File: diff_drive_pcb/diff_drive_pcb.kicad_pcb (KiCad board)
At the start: 2 copper layers, 13 parts, among them J1 Conn_01x02_Pin, J10 Conn_01x02_Pin, J2 Conn_01x04_Socket, J3 Conn_01x02_Pin, J4 Conn_01x04_Socket, J5 Conn_01x02_Pin, J6 Conn_01x04_Socket, J7 Conn_01x02_Pin, J8 Conn_01x04_Socket, J9 Conn_01x02_Pin, U1 TB6612FNG, U2 TB6612FNG, U3 Teensy4.1

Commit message: PCB v1.0 developed
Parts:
- added BZ1: Buzzer, Buzzer_Beeper:Buzzer_TDK_PS1240P02BT_D12.2mm_H6.5mm, F.Cu at (167.5, 143.9)
- added BZ3: Buzzer, Buzzer_Beeper:Buzzer_TDK_PS1240P02BT_D12.2mm_H6.5mm, F.Cu at (149.5, 143.9)
- added D1: 1N5400, Diode_THT:D_DO-201AD_P15.24mm_Horizontal, F.Cu at (204.7, 56.4)
- added D2: 1N5400, Diode_THT:D_DO-201AD_P15.24mm_Horizontal, F.Cu at (210.6, 56.4)
- added D3: status_led1, Connector_PinHeader_2.54mm:PinHeader_1x02_P2.54mm_Vertical, F.Cu at (175.5, 65.9)
- added D4: status_led2, Connector_PinHeader_2.54mm:PinHeader_1x02_P2.54mm_Vertical, F.Cu at (175.5, 69.9)
- added D5: status_led3, Connector_PinHeader_2.54mm:PinHeader_1x02_P2.54mm_Vertical, F.Cu at (175.5, 73.9)
- added D6: headlight, Connector_PinHeader_2.54mm:PinHeader_1x02_P2.54mm_Vertical, F.Cu at (138.5, 102.9)
- added J11: Motor_Break_SW, Connector_PinHeader_2.54mm:PinHeader_1x03_P2.54mm_Vertical, F.Cu at (146.0, 120.5)
- added J12: 5v_out_1, Connector_JST:JST_XH_B2B-XH-A_1x02_P2.50mm_Vertical, F.Cu at (196.0, 57.4)
- added J13: 5v_out_2, Connector_JST:JST_XH_B2B-XH-A_1x02_P2.50mm_Vertical, F.Cu at (196.0, 64.4)
- added J14: 5v_out_3, Connector_JST:JST_XH_B2B-XH-A_1x02_P2.50mm_Vertical, F.Cu at (196.0, 71.4)
- added J15: 5v_out_4, Connector_JST:JST_XH_B2B-XH-A_1x02_P2.50mm_Vertical, F.Cu at (196.0, 78.4)
- added J16: 3v3_out_1, Connector_JST:JST_XH_B2B-XH-A_1x02_P2.50mm_Vertical, F.Cu at (187.0, 71.4)
- added J17: 3v3_out_2, Connector_JST:JST_XH_B2B-XH-A_1x02_P2.50mm_Vertical, F.Cu at (187.0, 78.4)
- added J18: 3v3_out_3, Connector_JST:JST_XH_B2B-XH-A_1x02_P2.50mm_Vertical, F.Cu at (187.0, 57.4)
- added J19: 3v3_out_4, Connector_JST:JST_XH_B2B-XH-A_1x02_P2.50mm_Vertical, F.Cu at (187.0, 64.4)
- added R1: 1K, Resistor_THT:R_Axial_DIN0204_L3.6mm_D1.6mm_P2.54mm_Vertical, F.Cu at (165.0, 66.6)
- added R2: 1K, Resistor_THT:R_Axial_DIN0204_L3.6mm_D1.6mm_P2.54mm_Vertical, F.Cu at (165.0, 69.8)
- added R3: 1K, Resistor_THT:R_Axial_DIN0204_L3.6mm_D1.6mm_P2.54mm_Vertical, F.Cu at (165.0, 72.9)
- added U4: TOF_front_left, Connector_JST:JST_XH_B6B-XH-AM_1x06_P2.50mm_Vertical, F.Cu at (113.1, 105.9)
- added U5: Tof_back_left, Connector_JST:JST_XH_B6B-XH-AM_1x06_P2.50mm_Vertical, F.Cu at (113.1, 123.4)
- added U6: Tof_front_right, Connector_JST:JST_XH_B6B-XH-AM_1x06_P2.50mm_Vertical, F.Cu at (113.1, 114.9)
- added U7: Tof_back_right, Connector_JST:JST_XH_B6B-XH-AM_1x06_P2.50mm_Vertical, F.Cu at (113.0, 132.9)
- added U8: MPU9250, Connector_PinHeader_2.54mm:PinHeader_1x10_P2.54mm_Vertical, F.Cu at (181.0, 85.4)
- J1: value Conn_01x02_Pin -> P_M1
- J10: value Conn_01x02_Pin -> 12V_IN
- J2: value Conn_01x04_Socket -> Encoder_M1
- J3: value Conn_01x02_Pin -> P_M2
- J4: value Conn_01x04_Socket -> Encoder_M2
- J5: value Conn_01x02_Pin -> P_M3
- J6: value Conn_01x04_Socket -> Encoder_M3
- J7: value Conn_01x02_Pin -> P_M4
- J8: value Conn_01x04_Socket -> Encoder_M4
- J9: value Conn_01x02_Pin -> 5V_IN
- U1: value TB6612FNG -> Motor Driver1; footprint Package_SO:SSOP-24_5.3x8.2mm_P0.65mm -> TB6612FNG:TB6612FNG breakout board
- U2: value TB6612FNG -> Motor Driver 2; footprint Package_SO:SSOP-24_5.3x8.2mm_P0.65mm -> TB6612FNG:TB6612FNG breakout board
- moved J5 89.5 mm to (109.5, 85.8)
- moved J8 87.6 mm to (182.5, 109.6), turned to -90 degrees
- moved J7 79.5 mm to (108.5, 96.8), turned to 90 degrees
- moved J2 64.7 mm to (172.5, 93.5), turned to -90 degrees
- moved J10 46.5 mm to (125.5, 40.5)
- moved J9 44.0 mm to (117.0, 40.5)
- moved U2 43.0 mm to (128.4, 90.0)
- moved J4 41.7 mm to (182.5, 93.4)
- moved J3 22.4 mm to (108.5, 77.2)
- moved J1 20.9 mm to (109.5, 65.8), turned to -90 degrees
- moved J6 16.2 mm to (172.5, 109.5)
- moved U3 10.7 mm to (153.9, 86.7)
- moved U1 6.47 mm to (128.4, 68.7)
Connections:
- U1 pad 1: /M1+ -> +12V
- U1 pad 10: Net-(U1-PGND2-Pad10) -> M1_ctrl_B
- U1 pad 11: /M2+ -> M1_ctrl_A
- U1 pad 12: /M2+ -> /Brk_sw
- U1 pad 13: unconnected-(U1-VM2-Pad13) -> M2_ctrl_A
- U1 pad 14: unconnected-(U1-VM3-Pad14) -> M2_ctrl_B
- U1 pad 15: unconnected-(U1-PWMB-Pad15) -> M2_ctrl_PWM
- U1 pad 16: unconnected-(U1-BIN2-Pad16) -> GND
- U1 pad 2: /M1+ -> +5V
- U1 pad 4: GND -> /M1+
- U1 pad 6: /M1- -> /M2-
- U1 pad 7: /M2- -> /M2+
- U1 pad 8: /M2- -> GND
- U1 pad 9: Net-(U1-PGND2-Pad10) -> M1_ctrl_PWM
- U2 pad 1: /M4+ -> +12V
- U2 pad 10: Net-(U2-PGND2-Pad10) -> M3_ctrl_B
- U2 pad 11: /M3+ -> M3_ctrl_A
- U2 pad 12: /M3+ -> /Brk_sw
- U2 pad 13: unconnected-(U2-VM2-Pad13) -> M4_ctrl_A
- U2 pad 14: unconnected-(U2-VM3-Pad14) -> M4_ctrl_B
- U2 pad 15: unconnected-(U2-PWMB-Pad15) -> M4_ctrl_PWM
- U2 pad 16: unconnected-(U2-BIN2-Pad16) -> GND
- U2 pad 2: /M4+ -> +5V
- U2 pad 4: GND -> /M3+
- U2 pad 5: /M4- -> /M3-
- U2 pad 7: /M3- -> /M4+
- U2 pad 8: /M3- -> GND
- U2 pad 9: Net-(U2-PGND2-Pad10) -> M3_ctrl_PWM
- U3 pad 10: M4_encB -> M3_ctrl_PWM
- U3 pad 11: M4_encA -> M3_ctrl_B
- U3 pad 12: unconnected-(U3-10_CS_MQSR-Pad12) -> M3_ctrl_A
- U3 pad 13: unconnected-(U3-11_MOSI_CTX1-Pad13) -> M4_ctrl_A
- U3 pad 14: unconnected-(U3-12_MISO_MQSL-Pad14) -> M4_ctrl_B
- U3 pad 16: unconnected-(U3-24_A10_TX6_SCL2-Pad16) -> M4_ctrl_PWM
- U3 pad 19: unconnected-(U3-27_A13_SCK1-Pad19) -> HEADLIGHTS
- U3 pad 20: unconnected-(U3-28_RX7-Pad20) -> XSHUT1
- U3 pad 21: unconnected-(U3-29_TX7-Pad21) -> XSHUT2
- U3 pad 22: unconnected-(U3-30_CRX3-Pad22) -> XSHUT3
- U3 pad 23: unconnected-(U3-31_CTX3-Pad23) -> XSHUT4
- U3 pad 24: unconnected-(U3-32_OUT1B-Pad24) -> /MD_stby
- U3 pad 25: unconnected-(U3-33_MCLK2-Pad25) -> M4_encA
- U3 pad 26: unconnected-(U3-34_RX8-Pad26) -> M4_encB
- U3 pad 27: unconnected-(U3-35_TX8-Pad27) -> M3_encA
- U3 pad 28: unconnected-(U3-36_CS-Pad28) -> M3_encB
- U3 pad 29: unconnected-(U3-37_CS-Pad29) -> M2_encA
- U3 pad 30: unconnected-(U3-38_CS1_IN1-Pad30) -> M2_encB
- U3 pad 31: unconnected-(U3-39_MISO1_OUT1A-Pad31) -> M1_encA
- U3 pad 32: unconnected-(U3-40_A16-Pad32) -> M1_encB
- U3 pad 38: unconnected-(U3-16_A2_RX4_SCL1-Pad38) -> MPU_SCL
- U3 pad 39: unconnected-(U3-17_A3_TX4_SDA1-Pad39) -> MPU_SDA
- U3 pad 4: M1_encB -> M1_ctrl_PWM
- U3 pad 42: unconnected-(U3-20_A6_TX5_LRCLK1-Pad42) -> STATUS_LED3
- U3 pad 43: unconnected-(U3-21_A7_RX5_BCLK1-Pad43) -> STATUS_LED2
- U3 pad 44: unconnected-(U3-22_A8_CTX1-Pad44) -> STATUS_LED1
- U3 pad 45: unconnected-(U3-23_A9_CRX1_MCLK1-Pad45) -> Buzzer_ctl
- U3 pad 46: unconnected-(U3-3V3-Pad46) -> +3V3
- U3 pad 5: M1_encA -> M1_ctrl_B
- U3 pad 6: M2_encB -> M1_ctrl_A
- U3 pad 7: M2_encA -> M2_ctrl_A
- U3 pad 8: M3_encB -> M2_ctrl_B
- U3 pad 9: M3_encA -> M2_ctrl_PWM
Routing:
- net GND: track 0.00 -> 466.7 mm
- net +5V: track 0.00 -> 399.4 mm
- net Buzzer_ctl: track 0.00 -> 127.4 mm
- net MPU_SDA: track 0.00 -> 101.6 mm
- net MPU_SCL: track 0.00 -> 98.0 mm
- net +3V3: track 0.00 -> 78.7 mm
- net /Brk_sw: track 0.00 -> 69.7 mm, vias 0 -> 1
- net +12V: track 0.00 -> 45.5 mm
- net Net-(D2-K): track 0.00 -> 44.5 mm
- net M4_encA: track 0.00 -> 30.2 mm
- net XSHUT4: track 0.00 -> 29.7 mm
- net M2_encA: track 0.00 -> 28.5 mm
- net Net-(D1-K): track 0.00 -> 27.6 mm
- net XSHUT3: track 0.00 -> 25.8 mm
- net M2_encB: track 0.00 -> 24.2 mm
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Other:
- board outline added: 114.5 x 119.5 mm
- board text added: "+12V_IN"
- board text added: "+3V3"
- board text added: "+5V"
- board text added: "+5V IN"
- board text added: "- +"
- board text added: "BL"
- board text added: "BR"
- board text added: "Brk_sw"
- board text added: "DIFF DRIVE CONTROLLER"
- board text added: "Designed By ShenLong"
- board text added: "E_M1"
- board text added: "E_M2"
- board text added: "E_M3"
- board text added: "E_M4"
- board text added: "FL"
- board text added: "FR"
- board text added: "L1"
- board text added: "L2"
- board text added: "L3"
- board text added: "M1_PWR"
- board text added: "M2_PWR"
- board text added: "M3_PWR"
- board text added: "M4_PWR"
- board text added: "MC_sw"
- board text added: "MOTOR ENCODER"
- board text added: "MPU_9250"
- board text added: "Motor_Break SW"
- board text added: "POWER OUTPUT"
- board text added: "Time of Flight"
- board text added: "v1.0"

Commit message: Updated Schematic
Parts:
- removed D1, D2: 1N5400, Diode_THT:D_DO-201AD_P15.24mm_Horizontal
- removed J12: 5v_out_1, Connector_JST:JST_XH_B2B-XH-A_1x02_P2.50mm_Vertical
- removed J13: 5v_out_2, Connector_JST:JST_XH_B2B-XH-A_1x02_P2.50mm_Vertical
- removed J14: 5v_out_3, Connector_JST:JST_XH_B2B-XH-A_1x02_P2.50mm_Vertical
- removed J15: 5v_out_4, Connector_JST:JST_XH_B2B-XH-A_1x02_P2.50mm_Vertical
- removed J16: 3v3_out_1, Connector_JST:JST_XH_B2B-XH-A_1x02_P2.50mm_Vertical
- removed J17: 3v3_out_2, Connector_JST:JST_XH_B2B-XH-A_1x02_P2.50mm_Vertical
- removed J18: 3v3_out_3, Connector_JST:JST_XH_B2B-XH-A_1x02_P2.50mm_Vertical
- removed J19: 3v3_out_4, Connector_JST:JST_XH_B2B-XH-A_1x02_P2.50mm_Vertical
- added D7: headlight, Connector_PinHeader_2.54mm:PinHeader_1x02_P2.54mm_Vertical, F.Cu at (92.5, 121.0)
- added Q2: IRLZ24, Package_TO_SOT_THT:TO-220-3_Vertical, F.Cu at (86.4, 105.5)
- added R4: 10k, Resistor_THT:R_Axial_DIN0204_L3.6mm_D1.6mm_P5.08mm_Horizontal, F.Cu at (95.5, 108.0)
- added R5: 100, Resistor_THT:R_Axial_DIN0204_L3.6mm_D1.6mm_P5.08mm_Horizontal, F.Cu at (93.2, 108.8)
- added R6: 100, Resistor_THT:R_Axial_DIN0204_L3.6mm_D1.6mm_P5.08mm_Horizontal, F.Cu at (89.2, 108.8)
- U1: value Motor Driver1 -> Motor Driver 1; footprint TB6612FNG:TB6612FNG breakout board -> MDD3A:MDD3A
- U2: footprint TB6612FNG:TB6612FNG breakout board -> MDD3A:MDD3A
- moved J11 110.6 mm to (73.1, 37.3), turned to 180 degrees
- moved U6 91.4 mm to (182.5, 55.4), turned to -90 degrees
- moved U7 90.9 mm to (182.5, 74.2), turned to -90 degrees
- moved U4 79.4 mm to (174.5, 55.5), turned to -90 degrees
- moved U5 78.6 mm to (174.5, 74.2), turned to -90 degrees
- moved J4 62.1 mm to (121.0, 101.8), turned to 90 degrees
- moved J2 57.5 mm to (115.0, 94.3)
- moved BZ1 48.3 mm to (129.5, 114.1), turned to -90 degrees
- moved D6 48.2 mm to (92.5, 117.2), turned to -90 degrees
- moved J9 47.3 mm to (163.8, 33.1), turned to -90 degrees
- moved U1 42.8 mm to (94.6, 42.3), turned to -90 degrees
- moved J1 41.6 mm to (83.4, 33.4)
- moved U2 40.9 mm to (94.4, 67.2), turned to -90 degrees
- moved J3 38.5 mm to (82.9, 48.4), turned to -90 degrees
- moved J5 37.3 mm to (83.1, 59.4)
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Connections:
- D6 pad 2: HEADLIGHTS -> Net-(D6-A)
- J11 pad 3: +5V -> GND
- U1 pad 1: +12V -> M1_ctrl_A
- U1 pad 10: M1_ctrl_B -> /M2-
- U1 pad 11: M1_ctrl_A -> +12V
- U1 pad 2: +5V -> M1_ctrl_B
- U1 pad 4: /M1+ -> /Brk_sw
- U1 pad 5: /M1- -> M2_ctrl_A
- U1 pad 6: /M2- -> M2_ctrl_B
- U1 pad 7: /M2+ -> /M1+
- U1 pad 8: GND -> /M1-
- U1 pad 9: M1_ctrl_PWM -> /M2+
- U2 pad 1: +12V -> M3_ctrl_A
- U2 pad 10: M3_ctrl_B -> /M4-
- U2 pad 11: M3_ctrl_A -> +12V
- U2 pad 2: +5V -> M3_ctrl_B
- U2 pad 4: /M3+ -> /Brk_sw
- U2 pad 5: /M3- -> M4_ctrl_A
- U2 pad 6: /M4- -> M4_ctrl_B
- U2 pad 7: /M4+ -> /M3+
- U2 pad 8: GND -> /M3-
- U2 pad 9: M3_ctrl_PWM -> /M4+
- U3 pad 10: M3_ctrl_PWM -> unconnected-(U3-8_TX2_IN1-Pad10)
- U3 pad 11: M3_ctrl_B -> M3_ctrl_A
- U3 pad 12: M3_ctrl_A -> M3_ctrl_B
- U3 pad 16: M4_ctrl_PWM -> unconnected-(U3-24_A10_TX6_SCL2-Pad16)
- U3 pad 20: XSHUT1 -> M1_encA
- U3 pad 21: XSHUT2 -> M1_encB
- U3 pad 22: XSHUT3 -> M2_encA
- U3 pad 23: XSHUT4 -> M2_encB
- U3 pad 29: M2_encA -> XSHUT4
- U3 pad 30: M2_encB -> XSHUT3
- U3 pad 31: M1_encA -> XSHUT2
- U3 pad 32: M1_encB -> XSHUT1
- U3 pad 4: M1_ctrl_PWM -> unconnected-(U3-2_OUT2-Pad4)
- U3 pad 48: unconnected-(U3-VIN-Pad48) -> +5V
- U3 pad 5: M1_ctrl_B -> M1_ctrl_A
- U3 pad 6: M1_ctrl_A -> M1_ctrl_B
- U3 pad 9: M2_ctrl_PWM -> unconnected-(U3-7_RX2_OUT1A-Pad9)
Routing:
- net GND: track 466.7 -> 0.00 mm
- net +5V: track 399.4 -> 0.00 mm
- net Buzzer_ctl: track 127.4 -> 0.00 mm
- net MPU_SDA: track 101.6 -> 0.00 mm
- net MPU_SCL: track 98.0 -> 0.00 mm
- net +3V3: track 78.7 -> 0.00 mm
- net /Brk_sw: track 69.7 -> 0.00 mm, vias 1 -> 0
- net +12V: track 45.5 -> 0.00 mm
- net Net-(D2-K): track 44.5 -> 0.00 mm
- net M4_encA: track 30.2 -> 0.00 mm
- net XSHUT4: track 29.7 -> 0.00 mm
- net M2_encA: track 28.5 -> 0.00 mm
- net Net-(D1-K): track 27.6 -> 0.00 mm
- net XSHUT3: track 25.8 -> 0.00 mm
- net M2_encB: track 24.2 -> 0.00 mm
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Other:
- board outline removed
- board text added: "STATUS LED"
- board text removed: "+12V_IN"
- board text removed: "+3V3"
- board text removed: "+5V"
- board text removed: "+5V IN"
- board text removed: "- +"
- board text removed: "Brk_sw"
- board text removed: "DIFF DRIVE CONTROLLER"
- board text removed: "Designed By ShenLong"
- board text removed: "E_M1"
- board text removed: "E_M2"
- board text removed: "E_M3"
- board text removed: "E_M4"
- board text removed: "L1"
- board text removed: "L2"
- board text removed: "L3"
- board text removed: "M1_PWR"
- board text removed: "M2_PWR"
- board text removed: "M3_PWR"
- board text removed: "M4_PWR"
- board text removed: "MC_sw"
- board text removed: "MOTOR ENCODER"
- board text removed: "MPU_9250"
- board text removed: "Motor_Break SW"
- board text removed: "POWER OUTPUT"
- board text removed: "Time of Flight"
- board text removed: "v1.0"

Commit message: Rev 2.1 pcb design
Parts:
- added J12: POWER_SW, Connector_JST:JST_XH_B2B-XH-AM_1x02_P2.50mm_Vertical, F.Cu at (125.4, 61.9)
- moved Q2 103.9 mm to (184.5, 71.2)
- moved D6 103.9 mm to (190.6, 83.0)
- moved D7 103.9 mm to (190.6, 86.7)
- moved R4 103.9 mm to (193.6, 73.7)
- moved R5 103.9 mm to (191.3, 74.5)
- moved R6 103.9 mm to (187.3, 74.5)
- moved U6 103.4 mm to (108.5, 127.5), turned to 0 degrees
- moved U7 99.9 mm to (108.4, 141.2), turned to 0 degrees
- moved U4 92.7 mm to (108.5, 120.6), turned to 0 degrees
- moved U5 89.3 mm to (108.5, 134.3), turned to 0 degrees
- moved J11 80.0 mm to (129.0, 94.5)
- moved J9 60.8 mm to (110.7, 62.8), turned to 180 degrees
- moved J4 58.6 mm to (179.5, 98.9), turned to -90 degrees
- moved J2 54.8 mm to (169.6, 98.9)
- moved J1 48.1 mm to (99.7, 78.7)
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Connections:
- J9 pad 1: +5V -> (no net)
- J9 pad 2: GND -> (no net)
- U3 pad 10: unconnected-(U3-8_TX2_IN1-Pad10) -> /MD_stby
- U3 pad 19: HEADLIGHTS -> XSHUT1
- U3 pad 20: M1_encA -> XSHUT2
- U3 pad 21: M1_encB -> XSHUT3
- U3 pad 22: M2_encA -> XSHUT4
- U3 pad 23: M2_encB -> Buzzer_ctl
- U3 pad 24: /MD_stby -> unconnected-(U3-32_OUT1B-Pad24)
- U3 pad 29: XSHUT4 -> M2_encA
- U3 pad 30: XSHUT3 -> M2_encB
- U3 pad 31: XSHUT2 -> M1_encA
- U3 pad 32: XSHUT1 -> M1_encB
- U3 pad 41: unconnected-(U3-19_A5_SCL-Pad41) -> STATUS_LED3
- U3 pad 42: STATUS_LED3 -> STATUS_LED2
- U3 pad 43: STATUS_LED2 -> STATUS_LED1
- U3 pad 44: STATUS_LED1 -> HEADLIGHTS
- U3 pad 45: Buzzer_ctl -> unconnected-(U3-23_A9_CRX1_MCLK1-Pad45)
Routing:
- net GND: track 0.00 -> 336.4 mm
- net +5V: track 0.00 -> 282.8 mm, vias 0 -> 2
- net MPU_SDA: track 0.00 -> 104.7 mm
- net MPU_SCL: track 0.00 -> 99.9 mm
- net HEADLIGHTS: track 0.00 -> 54.3 mm
- net Buzzer_ctl: track 0.00 -> 41.5 mm
- net /Brk_sw: track 0.00 -> 41.2 mm
- net +12V: track 0.00 -> 36.8 mm
- net XSHUT4: track 0.00 -> 31.6 mm
- net M2_encB: track 0.00 -> 28.4 mm
- net M2_encA: track 0.00 -> 28.2 mm
- net XSHUT3: track 0.00 -> 27.3 mm
- net M4_encA: track 0.00 -> 26.8 mm
- net M4_encB: track 0.00 -> 26.8 mm
- net M3_ctrl_A: track 0.00 -> 25.9 mm
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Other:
- board outline added: 111 x 110.7 mm
- board text added: "HEADLIGHT"
- board text added: "IMU"

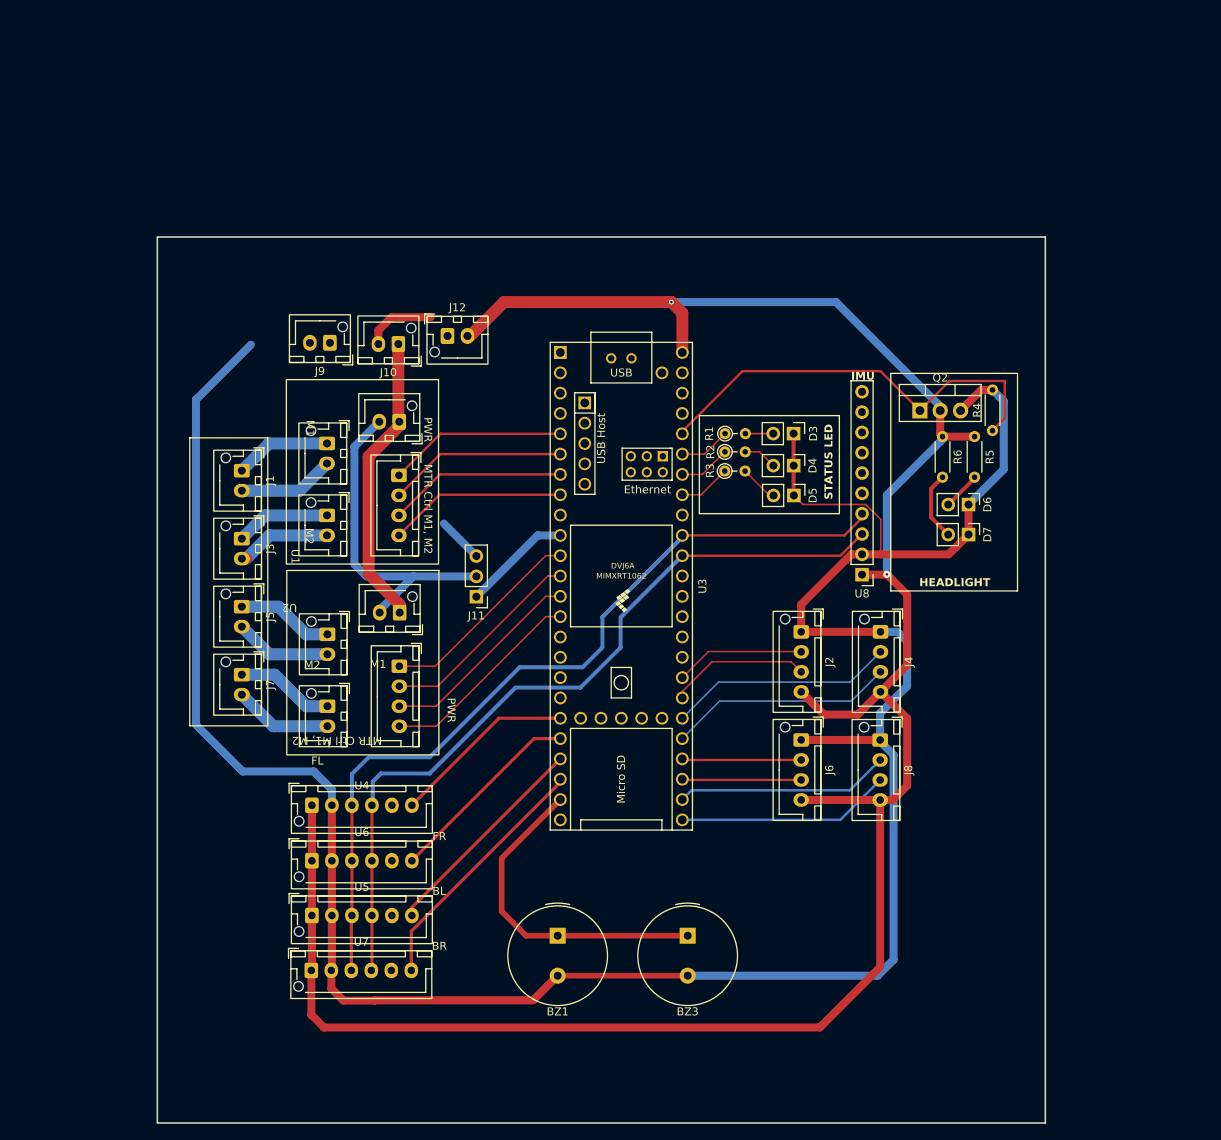
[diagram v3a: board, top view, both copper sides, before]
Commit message: Cleaned up PCB and adjusted size
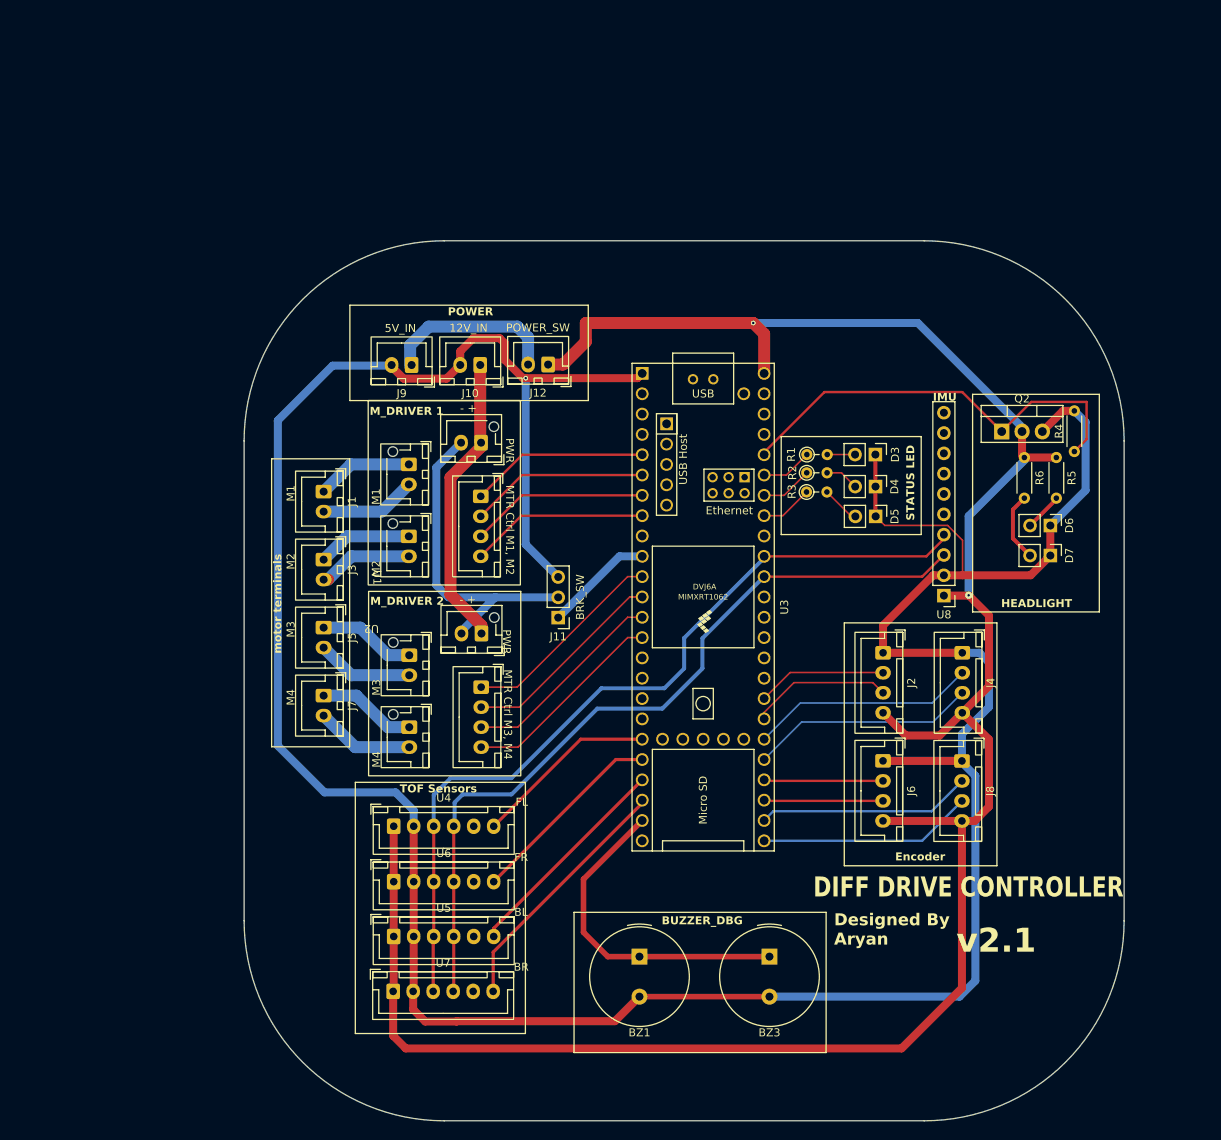
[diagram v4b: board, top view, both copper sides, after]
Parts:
- J1, J10, J12, J3, J5, J7, J9: footprint Connector_JST:JST_XH_B2B-XH-AM_1x02_P2.50mm_Vertical -> Connector_JST:JST_XH_B2B-XH-A_1x02_P2.50mm_Vertical
- J2, J4, J6, J8: footprint Connector_JST:JST_XH_B4B-XH-AM_1x04_P2.50mm_Vertical -> Connector_JST:JST_XH_B4B-XH-A_1x04_P2.50mm_Vertical
- U4, U5, U6, U7: footprint Connector_JST:JST_XH_B6B-XH-AM_1x06_P2.50mm_Vertical -> Connector_JST:JST_XH_B6B-XH-A_1x06_P2.50mm_Vertical
- moved J12 13.1 mm to (138.0, 65.5), turned to 180 degrees
- moved J9 10.6 mm to (120.9, 65.5)
- moved U5 10.6 mm to (118.7, 137.0)
- moved U6 10.6 mm to (118.7, 130.1)
- moved D3 10.6 mm to (178.9, 76.7)
- moved D4 10.6 mm to (178.9, 80.7)
- moved D6 10.6 mm to (200.8, 85.6)
- moved D7 10.6 mm to (200.8, 89.3)
- moved J6 10.6 mm to (179.9, 115.0)
- moved R1 10.6 mm to (170.3, 76.7)
- moved R3 10.6 mm to (170.3, 81.4)
- moved R4 10.6 mm to (203.8, 76.3)
- moved R5 10.6 mm to (201.5, 77.1)
- moved R6 10.6 mm to (197.5, 77.1)
- moved U1 10.6 mm to (123.5, 83.0)
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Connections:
- J12 pad 1: mc_power -> +5V
- J12 pad 2: +5V -> mc_power
- J9 pad 1: (no net) -> mc_power
- J9 pad 2: (no net) -> GND
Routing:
- net GND: track 336.4 -> 395.2 mm, vias 0 -> 1
- net mc_power: track 0.00 -> 22.6 mm
- net +5V: track 282.8 -> 284.7 mm
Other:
- board size 111 x 110.7 mm -> 110 x 110 mm
- board text added: "- +"
- board text added: "12V_IN"
- board text added: "5V_IN"
- board text added: "BRK_SW"
- board text added: "BUZZER_DBG"
- board text added: "DIFF DRIVE CONTROLLER"
- board text added: "Designed By Aryan"
- board text added: "Encoder"
- board text added: "M1"
- board text added: "M2"
- board text added: "M3"
- board text added: "M4"
- board text added: "M_DRIVER 1"
- board text added: "M_DRIVER 2"
- board text added: "POWER"
- board text added: "POWER_SW"
- board text added: "TOF Sensors"
- board text added: "motor terminals"
- board text added: "v2.1"
